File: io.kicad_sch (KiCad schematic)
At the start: 12 parts, among them J1 USB_C_Receptacle, J2 MEM2067-02-180-00-A, U3 USBLC6-2P6

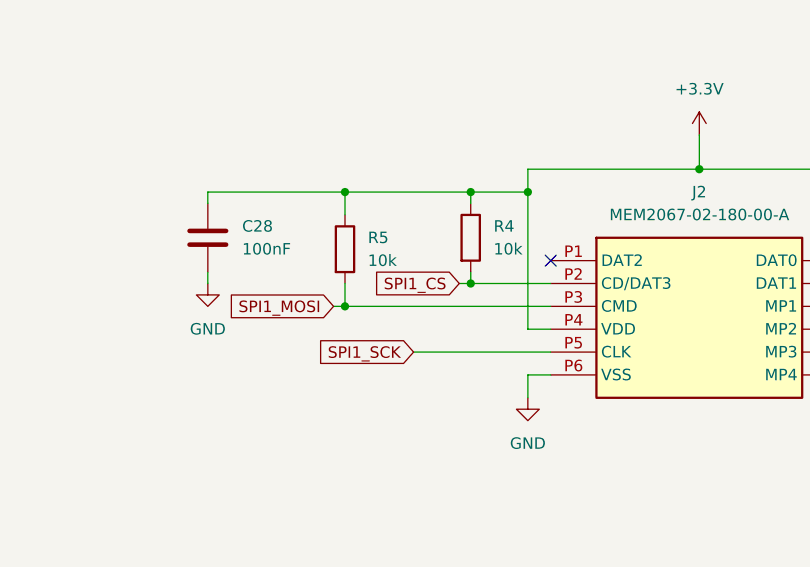
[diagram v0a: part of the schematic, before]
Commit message: Added all sensors and telemetry modem
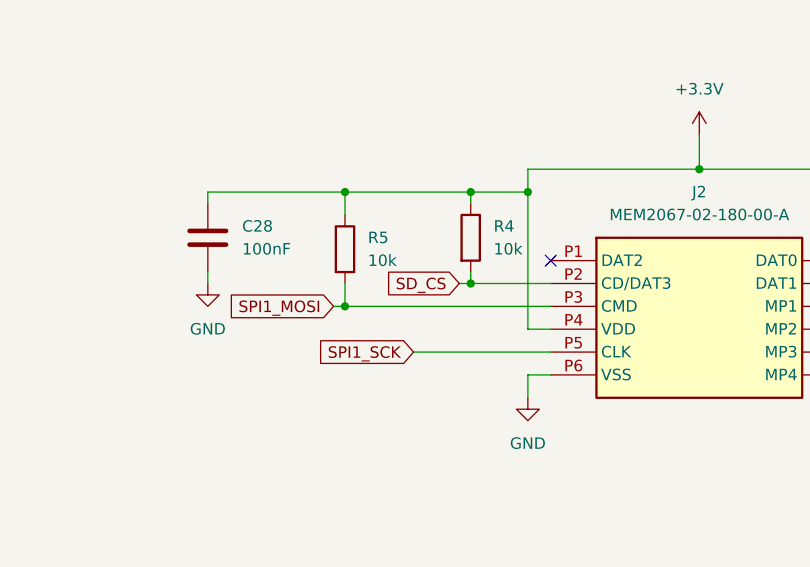
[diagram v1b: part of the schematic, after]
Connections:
- net SPI1_CS renamed SD_CS
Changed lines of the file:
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@@
 		)
 	)
-	(global_label "SPI1_CS"
+	(global_label "SD_CS"
 		(shape input)
 		(at 172.72 46.99 180)
@@
 		)
 		(property "Intersheetrefs" "${INTERSHEET_REFS}"
-			(at 161.9939 46.99 0)
+			(at 163.8082 46.99 0)
 			(effects
 				(font

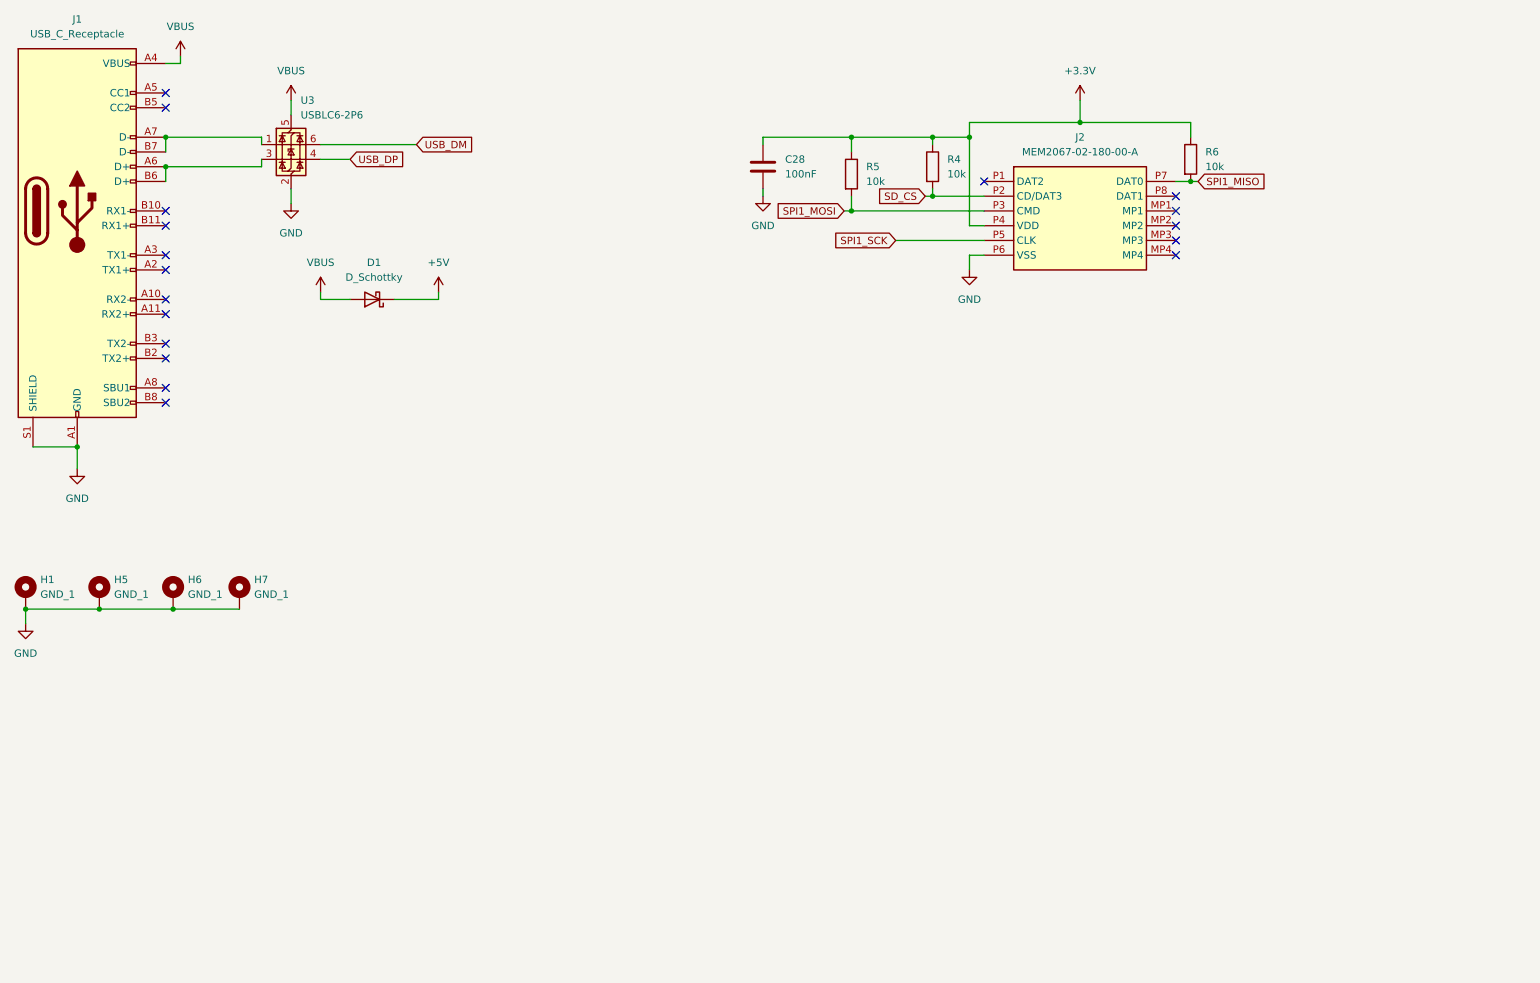
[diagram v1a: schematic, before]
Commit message: Added IO
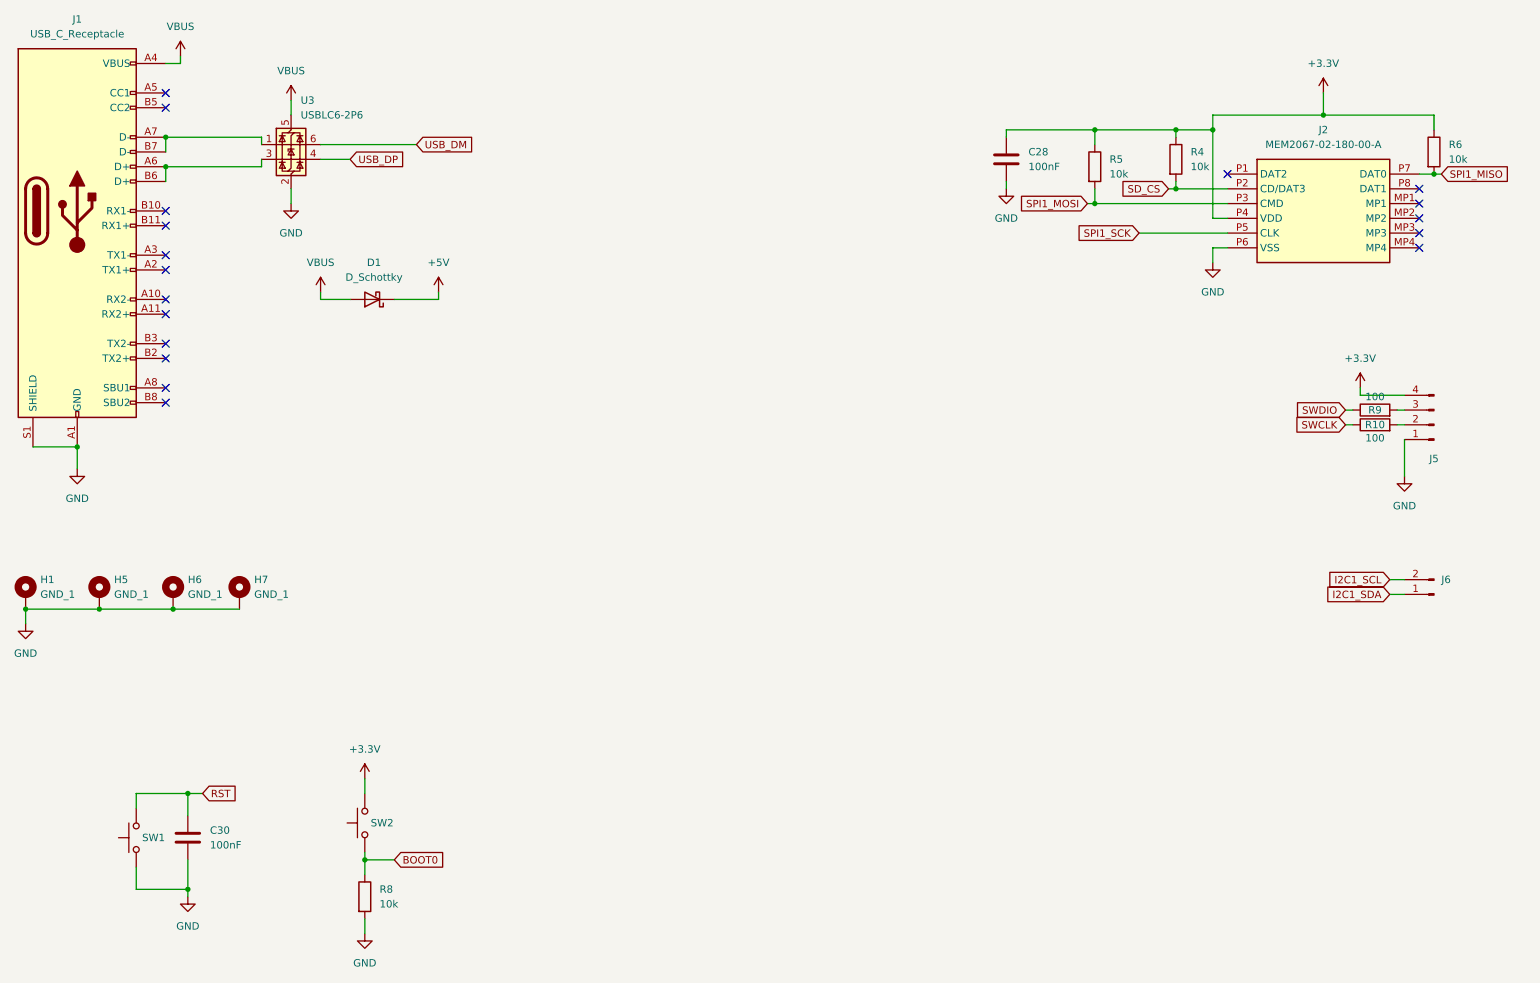
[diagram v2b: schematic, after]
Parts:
- added C30: 100nF, Capacitor_SMD:C_0201_0603Metric, symbol Device:C
- added J5: Conn_01x04_Pin, Connector_PinSocket_2.54mm:PinSocket_1x04_P2.54mm_Vertical, symbol Connector:Conn_01x04_Pin
- added J6: Conn_01x02_Pin, Connector_PinHeader_2.54mm:PinHeader_1x02_P2.54mm_Vertical, symbol Connector:Conn_01x02_Pin
- added R10, R9: 100, Resistor_SMD:R_0402_1005Metric, symbol Device:R
- added R8: 10k, Resistor_SMD:R_0201_0603Metric, symbol Device:R
- added SW1, SW2: SW_Push, Button_Switch_SMD:SW_SPST_PTS810, symbol Switch:SW_Push
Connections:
- net +3.3V: now also J5.4 (Pin_4), SW2.2
- net GND: now also C30.2, J5.1 (Pin_1), R8.2, SW1.1
- new net: J5.3 (Pin_3), R9.2
- new net: J5.2 (Pin_2), R10.2
- new net BOOT0: R8.1, SW2.1
- new net I2C1_SCL: J6.2 (Pin_2)
- new net I2C1_SDA: J6.1 (Pin_1)
- new net RST: C30.1, SW1.2
- new net SWCLK: R10.1
- new net SWDIO: R9.1
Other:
- moved on the sheet: C28, J2, R4, R5, R6

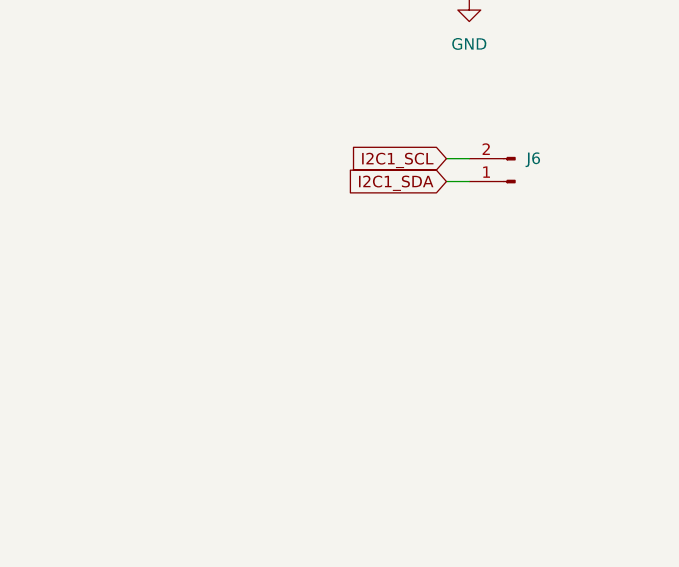
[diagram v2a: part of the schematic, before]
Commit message: Change 0201 to 0403
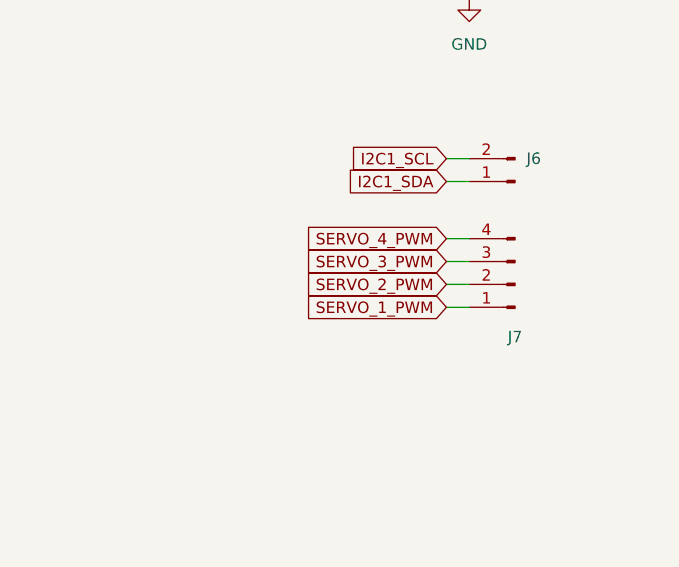
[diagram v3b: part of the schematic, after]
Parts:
- added J7: Conn_01x04_Pin, Connector_PinSocket_2.54mm:PinSocket_1x04_P2.54mm_Vertical, symbol Connector:Conn_01x04_Pin
- C28, C30: footprint Capacitor_SMD:C_0201_0603Metric -> Capacitor_SMD:C_0402_1005Metric
- D1: footprint Diode_SMD:D_0201_0603Metric -> Diode_SMD:D_0402_1005Metric
- R4, R5, R6, R8: footprint Resistor_SMD:R_0201_0603Metric -> Resistor_SMD:R_0402_1005Metric
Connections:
- new net SERVO_1_PWM: J7.1 (Pin_1)
- new net SERVO_2_PWM: J7.2 (Pin_2)
- new net SERVO_3_PWM: J7.3 (Pin_3)
- new net SERVO_4_PWM: J7.4 (Pin_4)
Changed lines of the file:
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@@
+	(wire
+		(pts
+			(xy 252.73 127) (xy 255.27 127)
+		)
+		(stroke
+			(width 0)
+			(type default)
+		)
+	)
 	(wire
 		(pts
@@
 	(wire
 		(pts
+			(xy 252.73 129.54) (xy 255.27 129.54)
+		)
+		(stroke
+			(width 0)
+			(type default)
+		)
+	)
+	(wire
+		(pts
 			(xy 222.25 55.88) (xy 222.25 58.42)
 		)
@@
 	(wire
 		(pts
+			(xy 252.73 124.46) (xy 255.27 124.46)
+		)
+		(stroke
+			(width 0)
+			(type default)
+		)
+	)
+	(wire
+		(pts
 			(xy 255.27 88.9) (xy 255.27 95.25)
 		)
@@
 		(pts
 			(xy 41.91 24.13) (xy 44.45 24.13)
+		)
+		(stroke
+			(width 0)
+			(type default)
+		)
+	)
+	(wire
+		(pts
+			(xy 252.73 121.92) (xy 255.27 121.92)
 		)
 		(stroke
@@
 		)
 	)
+	(global_label "SERVO_4_PWM"
+		(shape input)
+		(at 252.73 121.92 180)
+		(fields_autoplaced yes)
+		(effects
+			(font
+				(size 1.27 1.27)
+			)
+			(justify right)
+		)
+		(property "Intersheetrefs" "${INTERSHEET_REFS}"
+			(at 236.3797 121.92 0)
+			(effects
+				(font
+					(size 1.27 1.27)
+				)
+				(justify right)
+				(hide yes)
+			)
+		)
+	)
+	(global_label "SERVO_2_PWM"
+		(shape input)
+		(at 252.73 127 180)
+		(fields_autoplaced yes)
+		(effects
+			(font
+				(size 1.27 1.27)
+			)
+			(justify right)
+		)
+		(property "Intersheetrefs" "${INTERSHEET_REFS}"
+			(at 236.3797 127 0)
+			(effects
+				(font
+					(size 1.27 1.27)
+				)
+				(justify right)
+				(hide yes)
+			)
+		)
+	)
 	(global_label "BOOT0"
 		(shape input)
@@
 		)
 	)
+	(global_label "SERVO_3_PWM"
+		(shape input)
+		(at 252.73 124.46 180)
+		(fields_autoplaced yes)
+		(effects
+			(font
+				(size 1.27 1.27)
+			)
+			(justify right)
+		)
+		(property "Intersheetrefs" "${INTERSHEET_REFS}"
+			(at 236.3797 124.46 0)
+			(effects
+				(font
+					(size 1.27 1.27)
+				)
+				(justify right)
+				(hide yes)
+			)
+		)
+	)
 	(global_label "SPI1_SCK"
 		(shape input)
@@
 		)
 	)
+	(global_label "SERVO_1_PWM"
+		(shape input)
+		(at 252.73 129.54 180)
+		(fields_autoplaced yes)
+		(effects
+			(font
+				(size 1.27 1.27)
+			)
+			(justify right)
+		)
+		(property "Intersheetrefs" "${INTERSHEET_REFS}"
+			(at 236.3797 129.54 0)
+			(effects
+				(font
+					(size 1.27 1.27)
+				)
+				(justify right)
+				(hide yes)
+			)
+		)
+	)
 	(global_label "USB_DP"
 		(shape input)
@@
 			)
 		)
-		(property "Footprint" "Diode_SMD:D_0201_0603Metric"
+		(property "Footprint" "Diode_SMD:D_0402_1005Metric"
 			(at 77.47 64.77 0)
 			(effects
@@
 			)
 		)
-		(property "Footprint" "Resistor_SMD:R_0201_0603Metric"
+		(property "Footprint" "Resistor_SMD:R_0402_1005Metric"
 			(at 214.122 40.64 90)
 			(effects
@@
 			)
 		)
-		(property "Footprint" "Capacitor_SMD:C_0201_0603Metric"
+		(property "Footprint" "Capacitor_SMD:C_0402_1005Metric"
 			(at 46.6852 161.29 0)
 			(effects
@@
 	)
 	(symbol
+		(lib_id "Connector:Conn_01x04_Pin")
+		(at 260.35 127 180)
+		(unit 1)
+		(exclude_from_sim no)
+		(in_bom yes)
+		(on_board yes)
+		(dnp no)
+		(property "Reference" "J7"
+			(at 260.35 132.842 0)
+			(effects
+				(font
+					(size 1.27 1.27)
+				)
+			)
+		)
+		(property "Value" "Conn_01x04_Pin"
+			(at 259.715 132.08 0)
+			(effects
+				(font
+					(size 1.27 1.27)
+				)
+				(hide yes)
+			)
+		)
+		(property "Footprint" "Connector_PinSocket_2.54mm:PinSocket_1x04_P2.54mm_Vertical"
+			(at 260.35 127 0)
+			(effects
+				(font
+					(size 1.27 1.27)
+				)
+				(hide yes)
+			)
+		)
+		(property "Datasheet" "~"
+			(at 260.35 127 0)
+			(effects
+				(font
+					(size 1.27 1.27)
+				)
+				(hide yes)
+			)
+		)
+		(property "Description" "Generic connector, single row, 01x04, script generated"
+			(at 260.35 127 0)
+			(effects
+				(font
+					(size 1.27 1.27)
+				)
+				(hide yes)
+			)
+		)
+		(pin "2"
+		)
+		(pin "4"
+		)
+		(pin "3"
+		)
+		(pin "1"
+		)
+		(instances
+			(project "VanguardFlightComputer"
+				(path "/8210c139-a891-4d19-b6af-0ce30997a2bf/1347638a-1f77-4117-846f-092a26f2e048"
+					(reference "J7")
+					(unit 1)
+				)
+			)
+		)
+	)
+	(symbol
 		(lib_id "Device:R")
 		(at 201.93 41.91 0)
@@
 			)
 		)
-		(property "Footprint" "Resistor_SMD:R_0201_0603Metric"
+		(property "Footprint" "Resistor_SMD:R_0402_1005Metric"
 			(at 200.152 41.91 90)
 			(effects
@@
 			)
 		)
-		(property "Footprint" "Resistor_SMD:R_0201_0603Metric"
+		(property "Footprint" "Resistor_SMD:R_0402_1005Metric"
 			(at 74.422 167.64 90)
 			(effects
@@
 			)
 		)
-		(property "Footprint" "Capacitor_SMD:C_0201_0603Metric"
+		(property "Footprint" "Capacitor_SMD:C_0402_1005Metric"
 			(at 187.6552 44.45 0)
 			(effects
@@
 			)
 		)
-		(property "Footprint" "Resistor_SMD:R_0201_0603Metric"
+		(property "Footprint" "Resistor_SMD:R_0402_1005Metric"
 			(at 258.572 39.37 90)
 			(effects

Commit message: Added STM32_MX Project, LED, Fixed DRC Violations
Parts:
- J2: footprint MEM20670218000A -> VanguardLib:MEM20670218000A
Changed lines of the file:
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@@
 			)
 		)
-		(property "Footprint" "MEM20670218000A"
+		(property "Footprint" "VanguardLib:MEM20670218000A"
 			(at 254 138.1 0)
 			(effects
